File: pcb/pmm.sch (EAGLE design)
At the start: 37 parts, among them IC3 STM32F042F4, J1 AUDIO_JACK_3.5MM_PTH, J2 FFC3B07-05-T, SW3 324_SW, SW4 324_SW, U2 USBC_16P, U4 XC6206_DEV

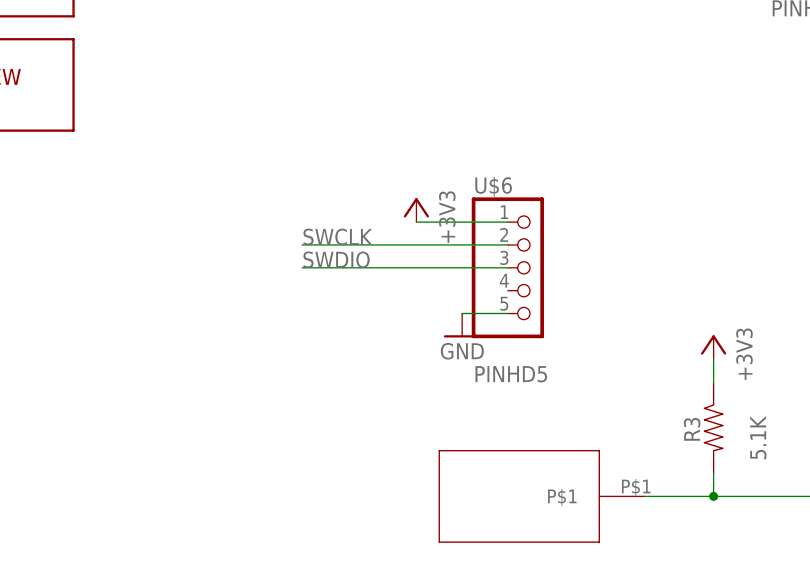
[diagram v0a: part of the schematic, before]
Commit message: light sensor PCB
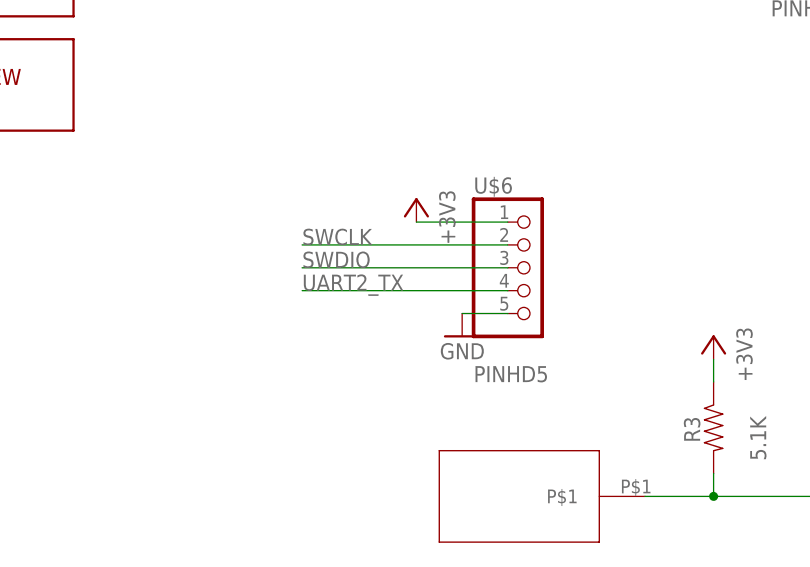
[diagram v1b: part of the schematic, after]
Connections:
- net UART2_TX: now also U$6.4
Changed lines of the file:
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@@
 <label x="-40.64" y="35.56" size="1.778" layer="95"/>
+</segment>
+<segment>
+<wire x1="-83.82" y1="30.48" x2="-106.68" y2="30.48" width="0.1524" layer="91"/>
+<pinref part="U$6" gate="G$1" pin="4"/>
+<label x="-106.68" y="30.48" size="1.778" layer="95"/>
 </segment>
 </net>

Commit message: shortened left side
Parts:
- removed U$9: PINHD1X2, adafruit_changed:PINHD1X2
- added JP2: (no value), adafruit_changed:PINHD-1X3CB
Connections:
- net +3V3: now also JP2.3
- net GND: now also JP2.2; no longer U$9.2
- net LIGHT_SENSE: now also JP2.1; no longer U$9.1
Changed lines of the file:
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@@
 <part name="GND17" library="supply1" deviceset="GND" device=""/>
 <part name="GND18" library="supply1" deviceset="GND" device=""/>
-<part name="U$9" library="adafruit_changed" deviceset="PINHD1X2" device=""/>
 <part name="GND19" library="supply1" deviceset="GND" device=""/>
 <part name="C3" library="clock" deviceset="CAP" device="0805" value="1uF"/>
 <part name="GND20" library="supply1" deviceset="GND" device=""/>
+<part name="JP2" library="adafruit_changed" deviceset="PINHD-1X3" device="CB"/>
+<part name="+3V9" library="supply1" library_urn="urn:adsk.eagle:library:371" deviceset="+3V3" device=""/>
 </parts>
 <sheets>
@@
 <attribute name="VALUE" x="2.54" y="-50.8" size="1.778" layer="96" rot="MR0"/>
 </instance>
-<instance part="U$9" gate="1" x="-48.26" y="66.04" smashed="yes">
-<attribute name="NAME" x="-54.61" y="71.755" size="1.778" layer="95"/>
-<attribute name="VALUE" x="-54.61" y="60.96" size="1.778" layer="96"/>
-</instance>
 <instance part="GND19" gate="1" x="-38.1" y="63.5" smashed="yes" rot="MR0">
 <attribute name="VALUE" x="-35.56" y="60.96" size="1.778" layer="96" rot="MR0"/>
@@
 <instance part="GND20" gate="1" x="360.68" y="20.32" smashed="yes" rot="MR0">
 <attribute name="VALUE" x="363.22" y="17.78" size="1.778" layer="96" rot="MR0"/>
+</instance>
+<instance part="JP2" gate="A" x="-55.88" y="66.04" smashed="yes">
+<attribute name="NAME" x="-62.23" y="71.755" size="1.778" layer="95"/>
+<attribute name="VALUE" x="-62.23" y="58.42" size="1.778" layer="96"/>
+</instance>
+<instance part="+3V9" gate="G$1" x="-68.58" y="66.04" smashed="yes" rot="MR0">
+<attribute name="VALUE" x="-66.04" y="60.96" size="1.778" layer="96" rot="MR90"/>
 </instance>
 </instances>
@@
 </segment>
 <segment>
-<pinref part="U$9" gate="1" pin="2"/>
 <pinref part="GND19" gate="1" pin="GND"/>
-<wire x1="-50.8" y1="66.04" x2="-38.1" y2="66.04" width="0.1524" layer="91"/>
+<wire x1="-58.42" y1="66.04" x2="-38.1" y2="66.04" width="0.1524" layer="91"/>
+<pinref part="JP2" gate="A" pin="2"/>
 </segment>
 <segment>
@@
 <pinref part="R6" gate="G$1" pin="2"/>
 <wire x1="35.56" y1="-5.08" x2="35.56" y2="-7.62" width="0.1524" layer="91"/>
+</segment>
+<segment>
+<pinref part="JP2" gate="A" pin="3"/>
+<pinref part="+3V9" gate="G$1" pin="+3V3"/>
+<wire x1="-58.42" y1="63.5" x2="-68.58" y2="63.5" width="0.1524" layer="91"/>
 </segment>
 </net>
@@
 <segment>
 <pinref part="J2" gate="G$1" pin="3"/>
-<wire x1="-10.16" y1="68.58" x2="-50.8" y2="68.58" width="0.1524" layer="91"/>
+<wire x1="-10.16" y1="68.58" x2="-58.42" y2="68.58" width="0.1524" layer="91"/>
 <label x="-38.1" y="68.58" size="1.778" layer="95"/>
-<pinref part="U$9" gate="1" pin="1"/>
-</segment>
-<segment>
+<pinref part="JP2" gate="A" pin="1"/>
+</segment>
+<segment>

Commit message: finishing touches
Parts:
- added TP1, TP2, TP3, TP4, TP5: TPTP12R, testpad:TPTP12R
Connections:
- net OLED_CS: now also TP1.TP
- net OLED_DC: now also TP2.TP
- net OLED_MOSI: now also TP4.TP
- net OLED_RESET: now also TP5.TP
- net OLED_SCK: now also TP3.TP
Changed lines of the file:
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@@
 <part name="JP2" library="adafruit_changed" deviceset="PINHD-1X3" device="CB"/>
 <part name="+3V9" library="supply1" library_urn="urn:adsk.eagle:library:371" deviceset="+3V3" device=""/>
+<part name="TP1" library="testpad" library_urn="urn:adsk.eagle:library:385" deviceset="TP" device="TP12R" package3d_urn="urn:adsk.eagle:package:27963/1" value="TPTP12R"/>
+<part name="TP2" library="testpad" library_urn="urn:adsk.eagle:library:385" deviceset="TP" device="TP12R" package3d_urn="urn:adsk.eagle:package:27963/1" value="TPTP12R"/>
+<part name="TP3" library="testpad" library_urn="urn:adsk.eagle:library:385" deviceset="TP" device="TP12R" package3d_urn="urn:adsk.eagle:package:27963/1" value="TPTP12R"/>
+<part name="TP4" library="testpad" library_urn="urn:adsk.eagle:library:385" deviceset="TP" device="TP12R" package3d_urn="urn:adsk.eagle:package:27963/1" value="TPTP12R"/>
+<part name="TP5" library="testpad" library_urn="urn:adsk.eagle:library:385" deviceset="TP" device="TP12R" package3d_urn="urn:adsk.eagle:package:27963/1" value="TPTP12R"/>
 </parts>
 <sheets>
@@
 <instance part="+3V9" gate="G$1" x="-68.58" y="66.04" smashed="yes" rot="MR0">
 <attribute name="VALUE" x="-66.04" y="60.96" size="1.778" layer="96" rot="MR90"/>
+</instance>
+<instance part="TP1" gate="G$1" x="0" y="139.7" smashed="yes">
+<attribute name="NAME" x="-1.27" y="140.97" size="1.778" layer="95"/>
+<attribute name="TP_SIGNAL_NAME" x="1.27" y="138.43" size="1.778" layer="97"/>
+</instance>
+<instance part="TP2" gate="G$1" x="-17.78" y="134.62" smashed="yes">
+<attribute name="NAME" x="-19.05" y="135.89" size="1.778" layer="95"/>
+<attribute name="TP_SIGNAL_NAME" x="-16.51" y="133.35" size="1.778" layer="97"/>
+</instance>
+<instance part="TP3" gate="G$1" x="-22.86" y="132.08" smashed="yes">
+<attribute name="NAME" x="-24.13" y="133.35" size="1.778" layer="95"/>
+<attribute name="TP_SIGNAL_NAME" x="-21.59" y="130.81" size="1.778" layer="97"/>
+</instance>
+<instance part="TP4" gate="G$1" x="-27.94" y="129.54" smashed="yes">
+<attribute name="NAME" x="-29.21" y="130.81" size="1.778" layer="95"/>
+<attribute name="TP_SIGNAL_NAME" x="-26.67" y="128.27" size="1.778" layer="97"/>
+</instance>
+<instance part="TP5" gate="G$1" x="-10.16" y="137.16" smashed="yes">
+<attribute name="NAME" x="-11.43" y="138.43" size="1.778" layer="95"/>
+<attribute name="TP_SIGNAL_NAME" x="-8.89" y="135.89" size="1.778" layer="97"/>
 </instance>
 </instances>
@@
 <pinref part="R8" gate="G$1" pin="1"/>
 <wire x1="38.1" y1="134.62" x2="99.06" y2="134.62" width="0.1524" layer="91"/>
-<wire x1="38.1" y1="134.62" x2="12.7" y2="134.62" width="0.1524" layer="91"/>
+<wire x1="38.1" y1="134.62" x2="-10.16" y2="134.62" width="0.1524" layer="91"/>
 <junction x="38.1" y="134.62"/>
 <label x="12.7" y="134.62" size="1.778" layer="95"/>
+<pinref part="TP5" gate="G$1" pin="TP"/>
 </segment>
 <segment>
@@
 <segment>
 <pinref part="U1" gate="G$1" pin="SDIN"/>
-<wire x1="38.1" y1="127" x2="12.7" y2="127" width="0.1524" layer="91"/>
 <label x="12.7" y="127" size="1.778" layer="95"/>
+<pinref part="TP4" gate="G$1" pin="TP"/>
+<wire x1="38.1" y1="127" x2="-27.94" y2="127" width="0.1524" layer="91"/>
 </segment>
 <segment>
@@
 <segment>
 <pinref part="U1" gate="G$1" pin="SCLK"/>
-<wire x1="38.1" y1="129.54" x2="12.7" y2="129.54" width="0.1524" layer="91"/>
+<wire x1="38.1" y1="129.54" x2="-22.86" y2="129.54" width="0.1524" layer="91"/>
 <label x="12.7" y="129.54" size="1.778" layer="95"/>
+<pinref part="TP3" gate="G$1" pin="TP"/>
 </segment>
 <segment>
@@
 <segment>
 <pinref part="U1" gate="G$1" pin="DC"/>
-<wire x1="38.1" y1="132.08" x2="12.7" y2="132.08" width="0.1524" layer="91"/>
 <label x="12.7" y="132.08" size="1.778" layer="95"/>
+<pinref part="TP2" gate="G$1" pin="TP"/>
+<wire x1="38.1" y1="132.08" x2="-17.78" y2="132.08" width="0.1524" layer="91"/>
 </segment>
 <segment>
@@
 <segment>
 <pinref part="U1" gate="G$1" pin="/CS"/>
-<wire x1="38.1" y1="137.16" x2="12.7" y2="137.16" width="0.1524" layer="91"/>
 <label x="12.7" y="137.16" size="1.778" layer="95"/>
+<pinref part="TP1" gate="G$1" pin="TP"/>
+<wire x1="38.1" y1="137.16" x2="0" y2="137.16" width="0.1524" layer="91"/>
 </segment>
 <segment>
@@
 will not be understood (or retained) with this version.
 </note>
+<note version="8.3" severity="warning">
+Since Version 8.3, EAGLE supports the association of 3D packages
+with devices in libraries, schematics, and board files. Those 3D
+packages will not be understood (or retained) with this version.
+</note>
 </compatibility>

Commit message: added pulldown on light sensor pin, pcb cleanup
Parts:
- removed TP1, TP2, TP3, TP4, TP5: TPTP12R, testpad:TPTP12R
- added R9: 10K, joyAnalog:RESISTOR0805-RES
- R3, R5, R6, R8: value 5.1K -> 10K
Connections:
- net GND: now also R9.2
- net LIGHT_SENSE: now also R9.1
- net OLED_CS: no longer TP1.TP
- net OLED_DC: no longer TP2.TP
- net OLED_MOSI: no longer TP4.TP
- net OLED_RESET: no longer TP5.TP
- net OLED_SCK: no longer TP3.TP
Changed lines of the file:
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@@
 <part name="R4" library="SparkFun-Passives" deviceset="RESISTOR" device="0805-RES" value="5K1"/>
 <part name="+3V2" library="supply1" library_urn="urn:adsk.eagle:library:371" deviceset="+3V3" device=""/>
-<part name="R5" library="joyAnalog" deviceset="RESISTOR" device="0805-RES" value="5.1K"/>
+<part name="R5" library="joyAnalog" deviceset="RESISTOR" device="0805-RES" value="10K"/>
 <part name="GND10" library="supply1" deviceset="GND" device=""/>
 <part name="U4" library="3pos_slide_switch" deviceset="XC6206_DEV" device=""/>
@@
 <part name="GND28" library="supply1" library_urn="urn:adsk.eagle:library:371" deviceset="GND" device=""/>
 <part name="GND29" library="supply1" library_urn="urn:adsk.eagle:library:371" deviceset="GND" device=""/>
-<part name="R8" library="joyAnalog" deviceset="RESISTOR" device="0805-RES" value="5.1K"/>
+<part name="R8" library="joyAnalog" deviceset="RESISTOR" device="0805-RES" value="10K"/>
 <part name="GND30" library="supply1" library_urn="urn:adsk.eagle:library:371" deviceset="GND" device=""/>
 <part name="BT1" library="BU2032SM-G" deviceset="BU2032SM-G" device=""/>
@@
 <part name="+3V4" library="supply1" library_urn="urn:adsk.eagle:library:371" deviceset="+3V3" device=""/>
 <part name="+3V5" library="supply1" library_urn="urn:adsk.eagle:library:371" deviceset="+3V3" device=""/>
-<part name="R3" library="joyAnalog" deviceset="RESISTOR" device="0805-RES" value="5.1K"/>
+<part name="R3" library="joyAnalog" deviceset="RESISTOR" device="0805-RES" value="10K"/>
 <part name="+3V8" library="supply1" library_urn="urn:adsk.eagle:library:371" deviceset="+3V3" device=""/>
 <part name="GND9" library="supply1" deviceset="GND" device=""/>
 <part name="+3V10" library="supply1" library_urn="urn:adsk.eagle:library:371" deviceset="+3V3" device=""/>
-<part name="R6" library="joyAnalog" deviceset="RESISTOR" device="0805-RES" value="5.1K"/>
+<part name="R6" library="joyAnalog" deviceset="RESISTOR" device="0805-RES" value="10K"/>
 <part name="U$8" library="adafruit_changed" deviceset="PINHD1X2" device=""/>
 <part name="GND17" library="supply1" deviceset="GND" device=""/>
@@
 <part name="JP2" library="adafruit_changed" deviceset="PINHD-1X3" device="CB"/>
 <part name="+3V9" library="supply1" library_urn="urn:adsk.eagle:library:371" deviceset="+3V3" device=""/>
-<part name="TP1" library="testpad" library_urn="urn:adsk.eagle:library:385" deviceset="TP" device="TP12R" package3d_urn="urn:adsk.eagle:package:27963/1" value="TPTP12R"/>
-<part name="TP2" library="testpad" library_urn="urn:adsk.eagle:library:385" deviceset="TP" device="TP12R" package3d_urn="urn:adsk.eagle:package:27963/1" value="TPTP12R"/>
-<part name="TP3" library="testpad" library_urn="urn:adsk.eagle:library:385" deviceset="TP" device="TP12R" package3d_urn="urn:adsk.eagle:package:27963/1" value="TPTP12R"/>
-<part name="TP4" library="testpad" library_urn="urn:adsk.eagle:library:385" deviceset="TP" device="TP12R" package3d_urn="urn:adsk.eagle:package:27963/1" value="TPTP12R"/>
-<part name="TP5" library="testpad" library_urn="urn:adsk.eagle:library:385" deviceset="TP" device="TP12R" package3d_urn="urn:adsk.eagle:package:27963/1" value="TPTP12R"/>
+<part name="R9" library="joyAnalog" deviceset="RESISTOR" device="0805-RES" value="10K"/>
+<part name="GND21" library="supply1" deviceset="GND" device=""/>
 </parts>
 <sheets>
@@
 <attribute name="VALUE" x="-104.14" y="-30.48" size="1.778" layer="96" rot="MR0"/>
 </instance>
-<instance part="GND4" gate="1" x="-88.9" y="25.4" smashed="yes" rot="MR0">
-<attribute name="VALUE" x="-86.36" y="22.86" size="1.778" layer="96" rot="MR0"/>
+<instance part="GND4" gate="1" x="-96.52" y="25.4" smashed="yes" rot="MR0">
+<attribute name="VALUE" x="-93.98" y="22.86" size="1.778" layer="96" rot="MR0"/>
 </instance>
 <instance part="U$6" gate="G$1" x="-81.28" y="30.48" smashed="yes">
@@
 <attribute name="VALUE" x="-66.04" y="60.96" size="1.778" layer="96" rot="MR90"/>
 </instance>
-<instance part="TP1" gate="G$1" x="0" y="139.7" smashed="yes">
-<attribute name="NAME" x="-1.27" y="140.97" size="1.778" layer="95"/>
-<attribute name="TP_SIGNAL_NAME" x="1.27" y="138.43" size="1.778" layer="97"/>
-</instance>
-<instance part="TP2" gate="G$1" x="-17.78" y="134.62" smashed="yes">
-<attribute name="NAME" x="-19.05" y="135.89" size="1.778" layer="95"/>
-<attribute name="TP_SIGNAL_NAME" x="-16.51" y="133.35" size="1.778" layer="97"/>
-</instance>
-<instance part="TP3" gate="G$1" x="-22.86" y="132.08" smashed="yes">
-<attribute name="NAME" x="-24.13" y="133.35" size="1.778" layer="95"/>
-<attribute name="TP_SIGNAL_NAME" x="-21.59" y="130.81" size="1.778" layer="97"/>
-</instance>
-<instance part="TP4" gate="G$1" x="-27.94" y="129.54" smashed="yes">
-<attribute name="NAME" x="-29.21" y="130.81" size="1.778" layer="95"/>
-<attribute name="TP_SIGNAL_NAME" x="-26.67" y="128.27" size="1.778" layer="97"/>
-</instance>
-<instance part="TP5" gate="G$1" x="-10.16" y="137.16" smashed="yes">
-<attribute name="NAME" x="-11.43" y="138.43" size="1.778" layer="95"/>
-<attribute name="TP_SIGNAL_NAME" x="-8.89" y="135.89" size="1.778" layer="97"/>
+<instance part="R9" gate="G$1" x="-27.94" y="63.5" smashed="yes" rot="MR270">
+<attribute name="NAME" x="-29.4386" y="64.77" size="1.778" layer="95" rot="MR270"/>
+<attribute name="VALUE" x="-22.098" y="64.77" size="1.778" layer="96" rot="MR270"/>
+</instance>
+<instance part="GND21" gate="1" x="-27.94" y="55.88" smashed="yes" rot="MR0">
+<attribute name="VALUE" x="-25.4" y="53.34" size="1.778" layer="96" rot="MR0"/>
 </instance>
 </instances>
@@
 <segment>
 <pinref part="GND4" gate="1" pin="GND"/>
-<wire x1="-88.9" y1="27.94" x2="-83.82" y2="27.94" width="0.1524" layer="91"/>
+<wire x1="-96.52" y1="27.94" x2="-83.82" y2="27.94" width="0.1524" layer="91"/>
 <pinref part="U$6" gate="G$1" pin="5"/>
 </segment>
@@
 <pinref part="C3" gate="G$1" pin="1"/>
 </segment>
+<segment>
+<pinref part="R9" gate="G$1" pin="2"/>
+<pinref part="GND21" gate="1" pin="GND"/>
+</segment>
 </net>
 <net name="+3V3" class="0">
@@
 <junction x="38.1" y="134.62"/>
 <label x="12.7" y="134.62" size="1.778" layer="95"/>
-<pinref part="TP5" gate="G$1" pin="TP"/>
 </segment>
 <segment>
@@
 <pinref part="U1" gate="G$1" pin="SDIN"/>
 <label x="12.7" y="127" size="1.778" layer="95"/>
-<pinref part="TP4" gate="G$1" pin="TP"/>
 <wire x1="38.1" y1="127" x2="-27.94" y2="127" width="0.1524" layer="91"/>
 </segment>
@@
 <wire x1="38.1" y1="129.54" x2="-22.86" y2="129.54" width="0.1524" layer="91"/>
 <label x="12.7" y="129.54" size="1.778" layer="95"/>
-<pinref part="TP3" gate="G$1" pin="TP"/>
 </segment>
 <segment>
@@
 <pinref part="U1" gate="G$1" pin="DC"/>
 <label x="12.7" y="132.08" size="1.778" layer="95"/>
-<pinref part="TP2" gate="G$1" pin="TP"/>
 <wire x1="38.1" y1="132.08" x2="-17.78" y2="132.08" width="0.1524" layer="91"/>
 </segment>
@@
 <pinref part="U1" gate="G$1" pin="/CS"/>
 <label x="12.7" y="137.16" size="1.778" layer="95"/>
-<pinref part="TP1" gate="G$1" pin="TP"/>
 <wire x1="38.1" y1="137.16" x2="0" y2="137.16" width="0.1524" layer="91"/>
 </segment>
@@
 <segment>
 <pinref part="J2" gate="G$1" pin="3"/>
-<wire x1="-10.16" y1="68.58" x2="-58.42" y2="68.58" width="0.1524" layer="91"/>
+<wire x1="-10.16" y1="68.58" x2="-27.94" y2="68.58" width="0.1524" layer="91"/>
 <label x="-38.1" y="68.58" size="1.778" layer="95"/>
 <pinref part="JP2" gate="A" pin="1"/>
+<pinref part="R9" gate="G$1" pin="1"/>
+<wire x1="-27.94" y1="68.58" x2="-58.42" y2="68.58" width="0.1524" layer="91"/>
+<junction x="-27.94" y="68.58"/>
 </segment>
 <segment>
@@
 will not be understood (or retained) with this version.
 </note>
-<note version="8.3" severity="warning">
-Since Version 8.3, EAGLE supports the association of 3D packages
-with devices in libraries, schematics, and board files. Those 3D
-packages will not be understood (or retained) with this version.
-</note>
 </compatibility>
